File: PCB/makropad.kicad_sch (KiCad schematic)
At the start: 53 parts, among them J1 OLED_DISPLAY, J2 Conn_01x04, J3 Conn_01x04, J4 Conn_01x04, J5 Conn_01x04, SW1 SW_Push_45deg, SW10 SW_Push_45deg, SW11 RotaryEncoder_Switch, SW12 RotaryEncoder_Switch, SW2 SW_Push_45deg, SW3 SW_Push_45deg, SW4 SW_Push_45deg, SW5 SW_Push_45deg, SW6 SW_Push_45deg, SW7 SW_Push_45deg, SW8 SW_Push_45deg, SW9 SW_Push_45deg, U1 PCF8574A, U2 MOUDLE-SEEEDUINO-XIAO

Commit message: feat: switch to SOD-123 diodes
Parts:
- D1, D10, D11, D12, D2, D3, D4, D5, D6, D7, D8, D9: footprint Diode_SMD:D_1206_3216Metric -> Diode_SMD:D_SOD-123
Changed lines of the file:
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@@
 			)
 		)
-		(property "Footprint" "Diode_SMD:D_1206_3216Metric"
+		(property "Footprint" "Diode_SMD:D_SOD-123"
 			(at 119.38 55.88 0)
 			(effects
@@
 			)
 		)
-		(property "Footprint" "Diode_SMD:D_1206_3216Metric"
+		(property "Footprint" "Diode_SMD:D_SOD-123"
 			(at 66.04 62.23 0)
 			(effects
@@
 			)
 		)
-		(property "Footprint" "Diode_SMD:D_1206_3216Metric"
+		(property "Footprint" "Diode_SMD:D_SOD-123"
 			(at 69.85 55.88 0)
 			(effects
@@
 			)
 		)
-		(property "Footprint" "Diode_SMD:D_1206_3216Metric"
+		(property "Footprint" "Diode_SMD:D_SOD-123"
 			(at 91.44 62.23 0)
 			(effects
@@
 			)
 		)
-		(property "Footprint" "Diode_SMD:D_1206_3216Metric"
+		(property "Footprint" "Diode_SMD:D_SOD-123"
 			(at 53.34 48.26 0)
 			(effects
@@
 			)
 		)
-		(property "Footprint" "Diode_SMD:D_1206_3216Metric"
+		(property "Footprint" "Diode_SMD:D_SOD-123"
 			(at 73.66 48.26 0)
 			(effects
@@
 			)
 		)
-		(property "Footprint" "Diode_SMD:D_1206_3216Metric"
+		(property "Footprint" "Diode_SMD:D_SOD-123"
 			(at 123.19 48.26 0)
 			(effects
@@
 			)
 		)
-		(property "Footprint" "Diode_SMD:D_1206_3216Metric"
+		(property "Footprint" "Diode_SMD:D_SOD-123"
 			(at 95.25 55.88 0)
 			(effects
@@
 			)
 		)
-		(property "Footprint" "Diode_SMD:D_1206_3216Metric"
+		(property "Footprint" "Diode_SMD:D_SOD-123"
 			(at 40.64 62.23 0)
 			(effects
@@
 			)
 		)
-		(property "Footprint" "Diode_SMD:D_1206_3216Metric"
+		(property "Footprint" "Diode_SMD:D_SOD-123"
 			(at 49.53 55.88 0)
 			(effects
@@
 			)
 		)
-		(property "Footprint" "Diode_SMD:D_1206_3216Metric"
+		(property "Footprint" "Diode_SMD:D_SOD-123"
 			(at 99.06 48.26 0)
 			(effects
@@
 			)
 		)
-		(property "Footprint" "Diode_SMD:D_1206_3216Metric"
+		(property "Footprint" "Diode_SMD:D_SOD-123"
 			(at 111.76 62.23 0)
 			(effects

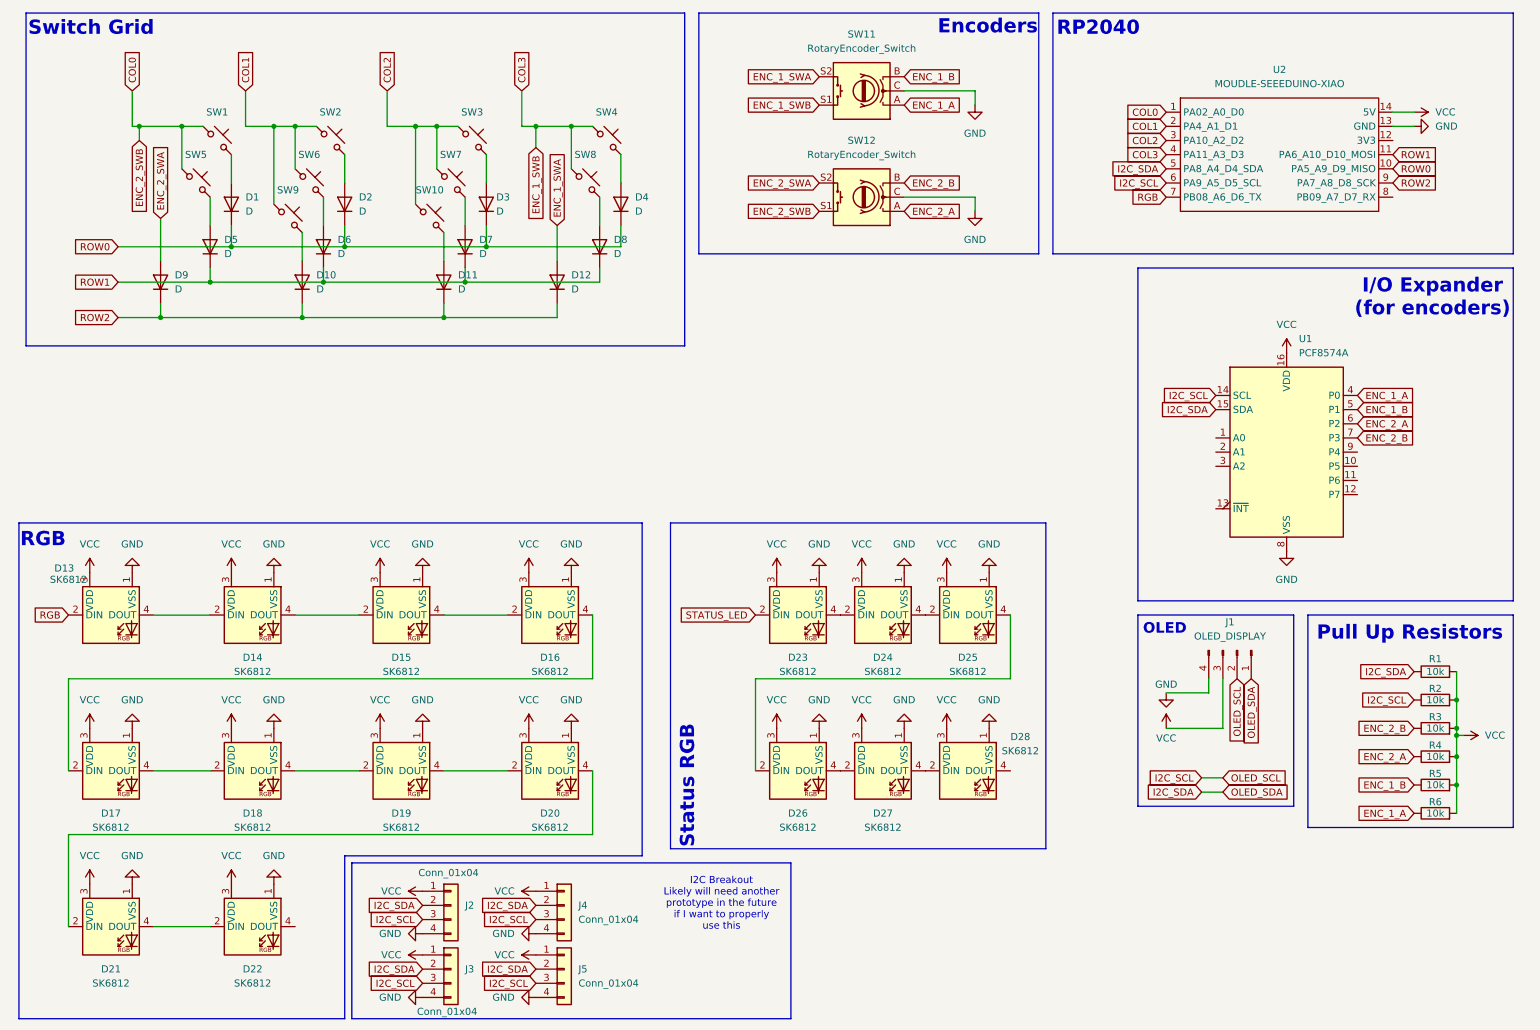
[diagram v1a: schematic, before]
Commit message: feat: switch to gateron low profile
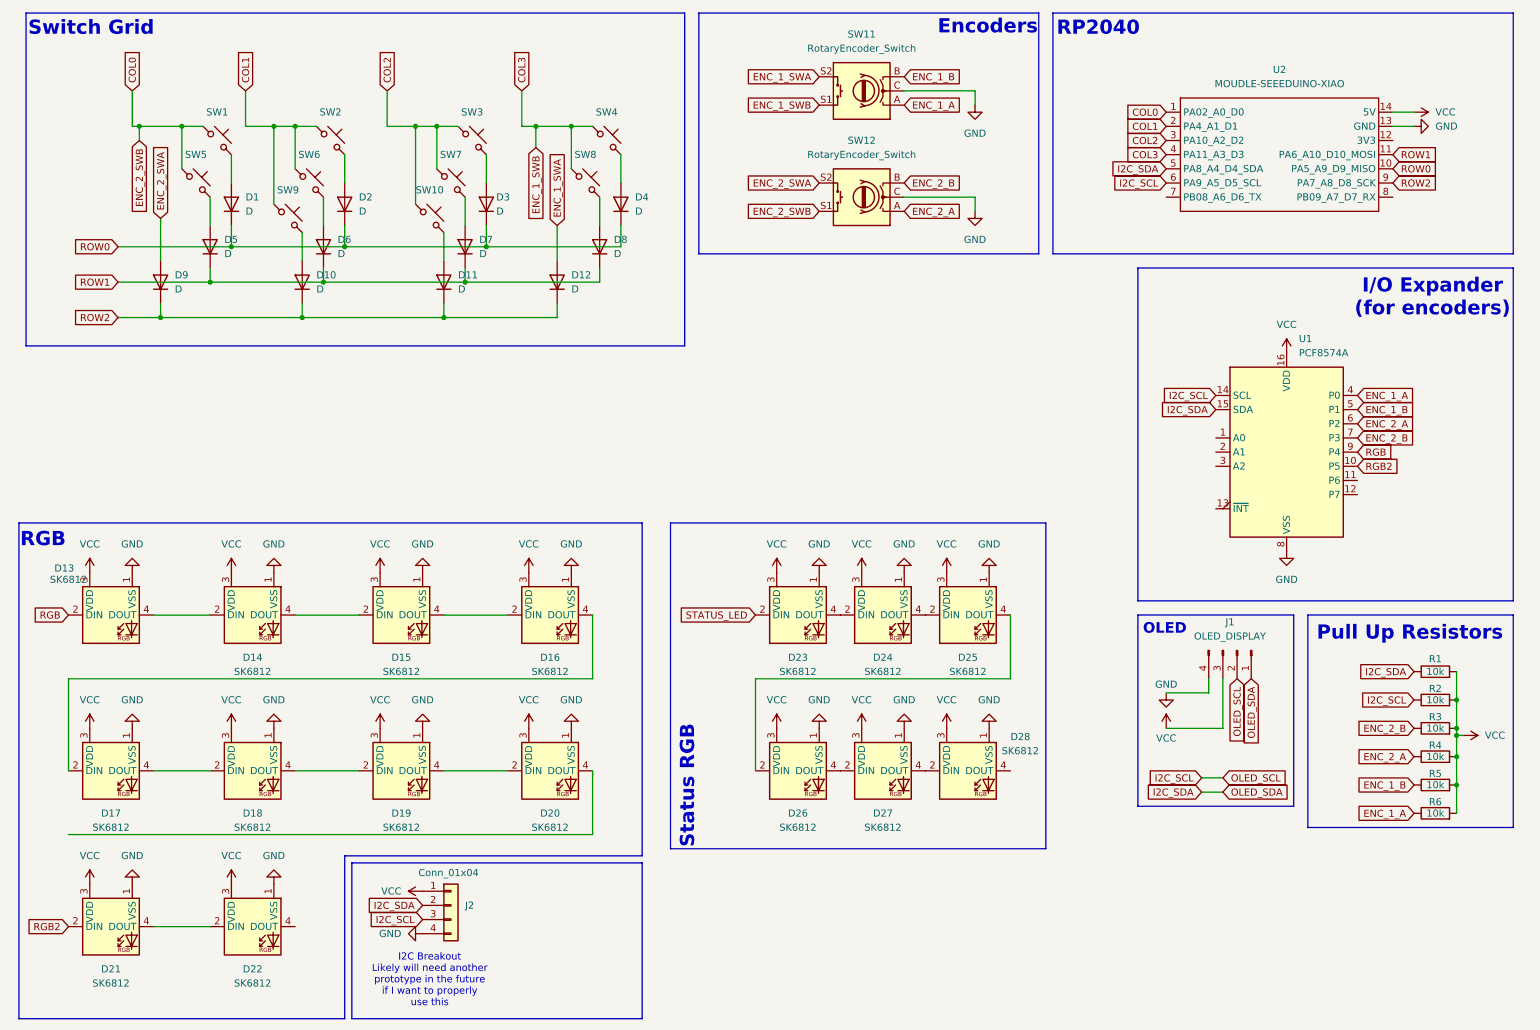
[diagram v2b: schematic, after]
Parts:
- removed J3, J4, J5: Conn_01x04, Components:4pin, symbol Connector_Generic:Conn_01x04
- SW1, SW10, SW2, SW3, SW4, SW5, SW6, SW7, SW8, SW9: footprint Components:MX-Solderable-1U -> Components:Gateron Low Profile Switch 2.0
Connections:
- net RGB: now also U1.9 (P4); no longer U2.7 (PB08_A6_D6_TX)
- net at D20.4 (DOUT): no longer D21.2 (DIN)
- net RGB2: now reaches U1.10 (P5)
- net RGB2: now also D21.2 (DIN)

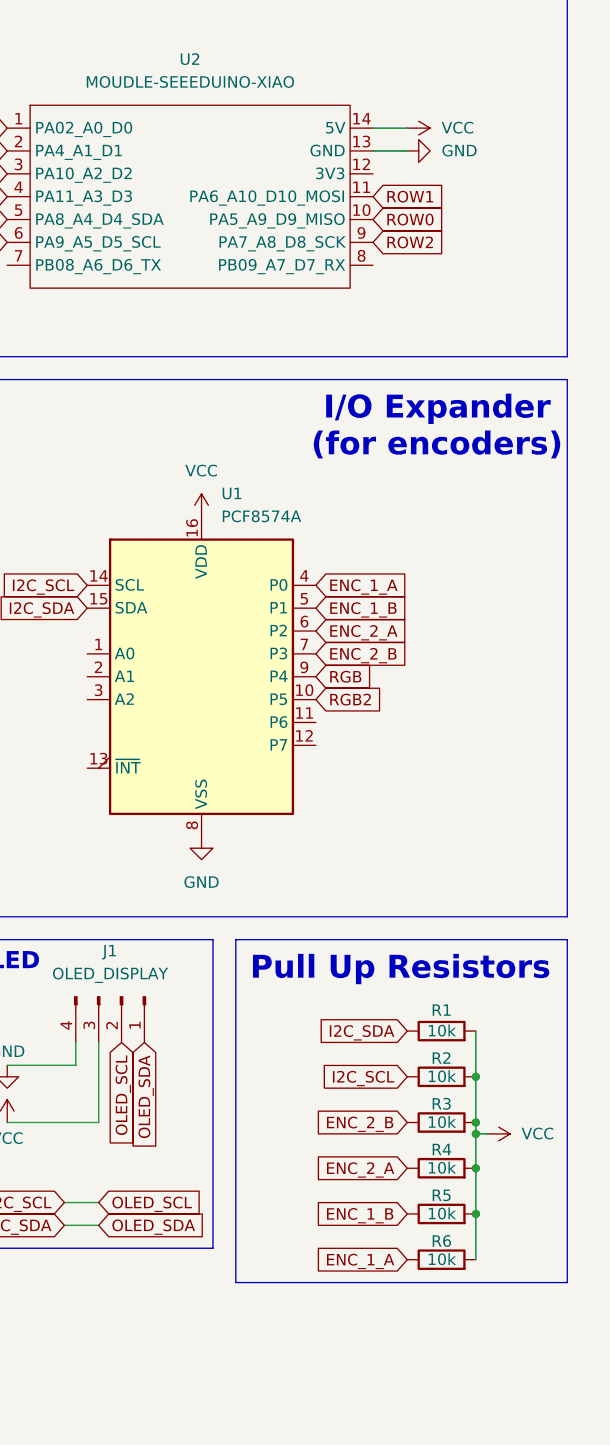
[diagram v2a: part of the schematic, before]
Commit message: feat: pull up i2c lines to 3.3v and remove encoder pull ups
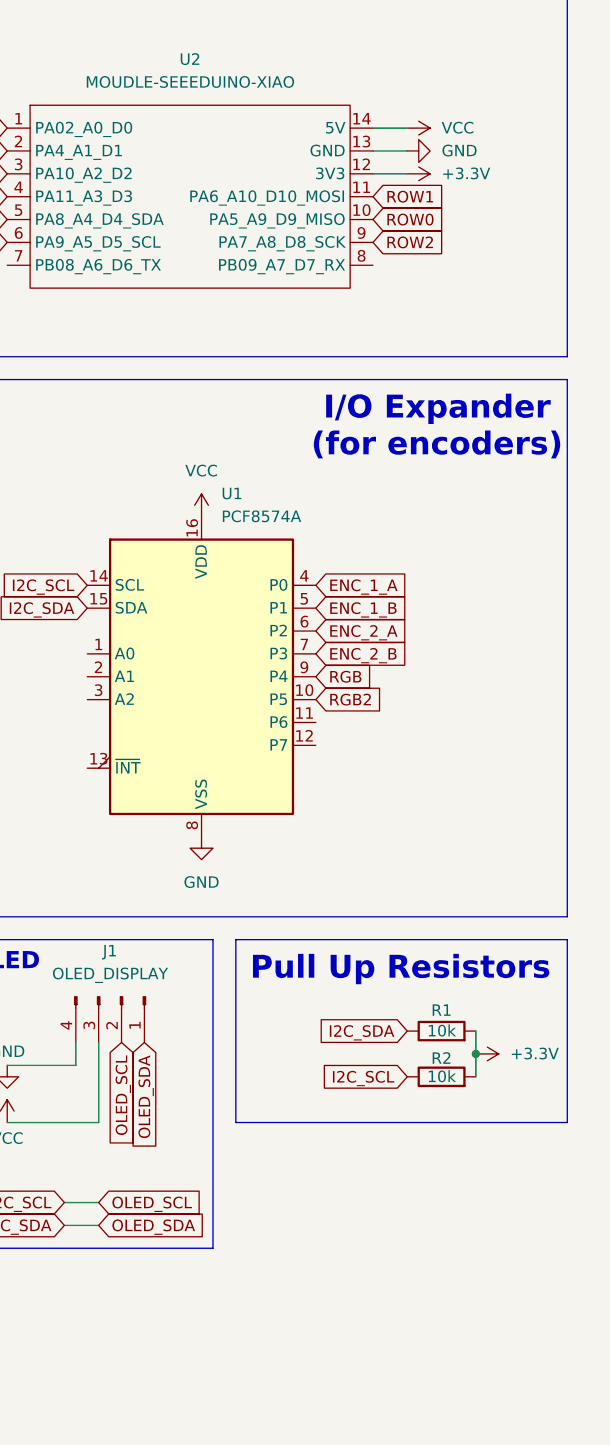
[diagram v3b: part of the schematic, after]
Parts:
- removed R3, R4, R5, R6: 10k, Resistor_SMD:R_1206_3216Metric, symbol Device:R
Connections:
- net VCC: no longer R1.2, R2.2
- net +3.3V: now reaches U2.12 (3V3)
- net +3.3V: now also R1.2, R2.2

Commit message: fuck
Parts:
- D13, D14, D15, D16, D17, D18, D19, D20, D21, D22: footprint Components:SK6812MINI-E -> Components:LED_SK6812MINI
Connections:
- net STATUS_LED: now also U1.11 (P6)
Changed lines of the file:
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@@
 		)
 	)
+	(global_label "STATUS_LED"
+		(shape input)
+		(at 255.27 97.79 0)
+		(fields_autoplaced yes)
+		(effects
+			(font
+				(size 1.27 1.27)
+			)
+			(justify left)
+		)
+		(property "Intersheetrefs" "${INTERSHEET_REFS}"
+			(at 269.4432 97.79 0)
+			(effects
+				(font
+					(size 1.27 1.27)
+				)
+				(justify left)
+				(hide yes)
+			)
+		)
+	)
 	(global_label "COL1"
 		(shape input)
@@
 			)
 		)
-		(property "Footprint" "Components:SK6812MINI-E"
+		(property "Footprint" "Components:LED_SK6812MINI"
 			(at 63.5 115.57 0)
 			(effects
@@
 			)
 		)
-		(property "Footprint" "Components:SK6812MINI-E"
+		(property "Footprint" "Components:LED_SK6812MINI"
 			(at 63.5 143.51 0)
 			(effects
@@
 			)
 		)
-		(property "Footprint" "Components:SK6812MINI-E"
+		(property "Footprint" "Components:LED_SK6812MINI"
 			(at 38.1 171.45 0)
 			(effects
@@
 			)
 		)
-		(property "Footprint" "Components:SK6812MINI-E"
+		(property "Footprint" "Components:LED_SK6812MINI"
 			(at 63.5 171.45 0)
 			(effects
@@
 			)
 		)
-		(property "Footprint" "Components:SK6812MINI-E"
+		(property "Footprint" "Components:LED_SK6812MINI"
 			(at 90.17 143.51 0)
 			(effects
@@
 			)
 		)
-		(property "Footprint" "Components:SK6812MINI-E"
+		(property "Footprint" "Components:LED_SK6812MINI"
 			(at 116.84 115.57 0)
 			(effects
@@
 			)
 		)
-		(property "Footprint" "Components:SK6812MINI-E"
+		(property "Footprint" "Components:LED_SK6812MINI"
 			(at 38.1 143.51 0)
 			(effects
@@
 			)
 		)
-		(property "Footprint" "Components:SK6812MINI-E"
+		(property "Footprint" "Components:LED_SK6812MINI"
 			(at 38.1 115.57 0)
 			(effects
@@
 			)
 		)
-		(property "Footprint" "Components:SK6812MINI-E"
+		(property "Footprint" "Components:LED_SK6812MINI"
 			(at 90.17 115.57 0)
 			(effects
@@
 			)
 		)
-		(property "Footprint" "Components:SK6812MINI-E"
+		(property "Footprint" "Components:LED_SK6812MINI"
 			(at 116.84 143.51 0)
 			(effects
